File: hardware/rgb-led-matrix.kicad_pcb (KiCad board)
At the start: 2 copper layers, 75 x 55 mm, 153 parts, among them J1 AKL_5_2, P1 CONN_01X02, P2 CON-SENSOR, Q1 2N7002P, U1 XMC1XXX24, U2 DRILL, U3 DRILL, U4 DRILL, U5 DRILL

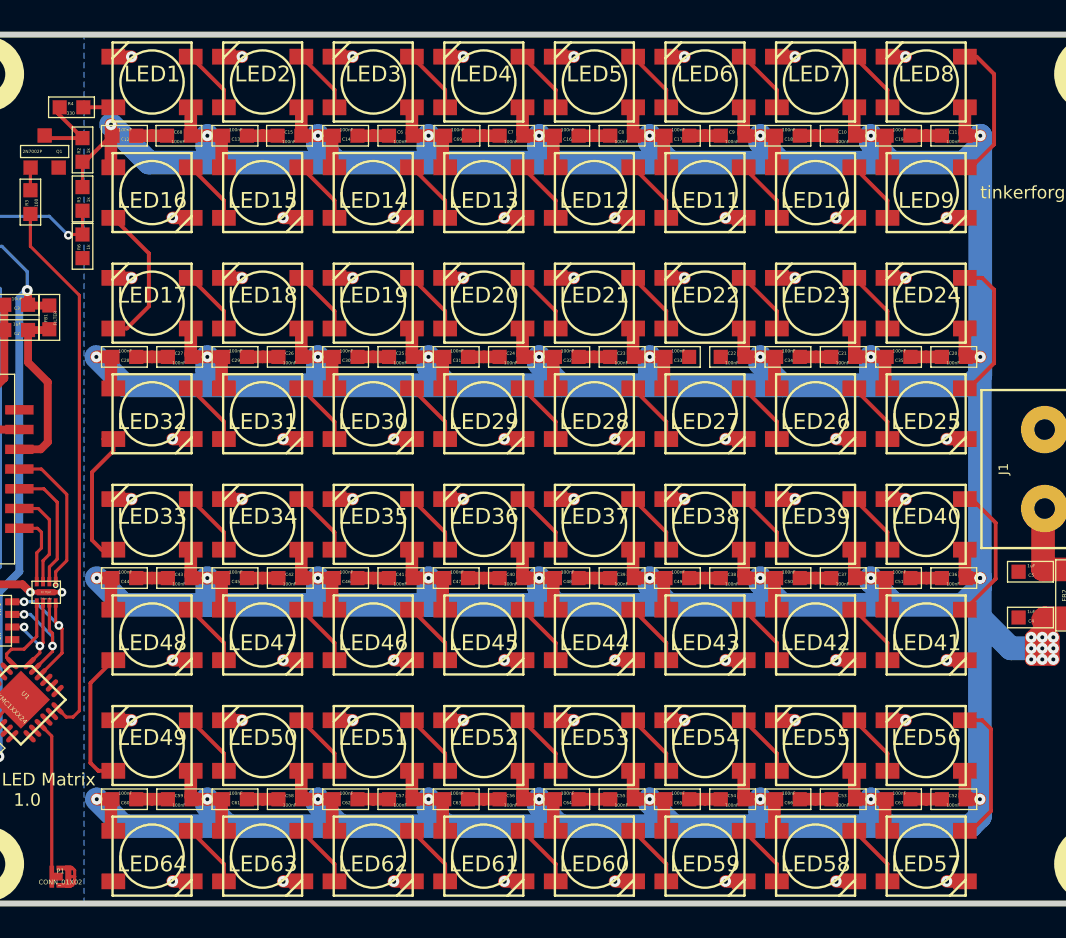
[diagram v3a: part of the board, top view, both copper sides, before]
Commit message: add vias for better cooling
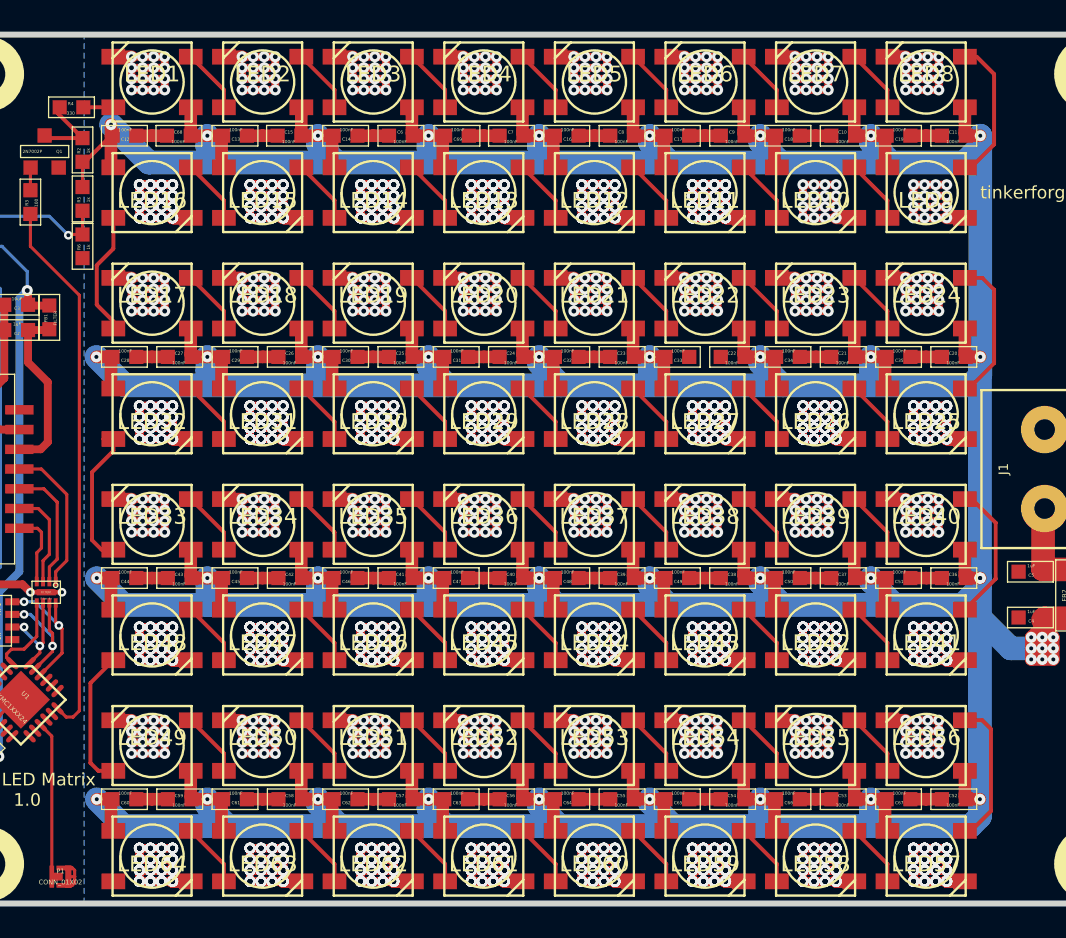
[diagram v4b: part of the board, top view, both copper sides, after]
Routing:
- net GND: track 160.4 -> 1880.9 mm, vias 71 -> 2471
- net Net-(LED16-Pad2): track 10.3 -> 8.82 mm

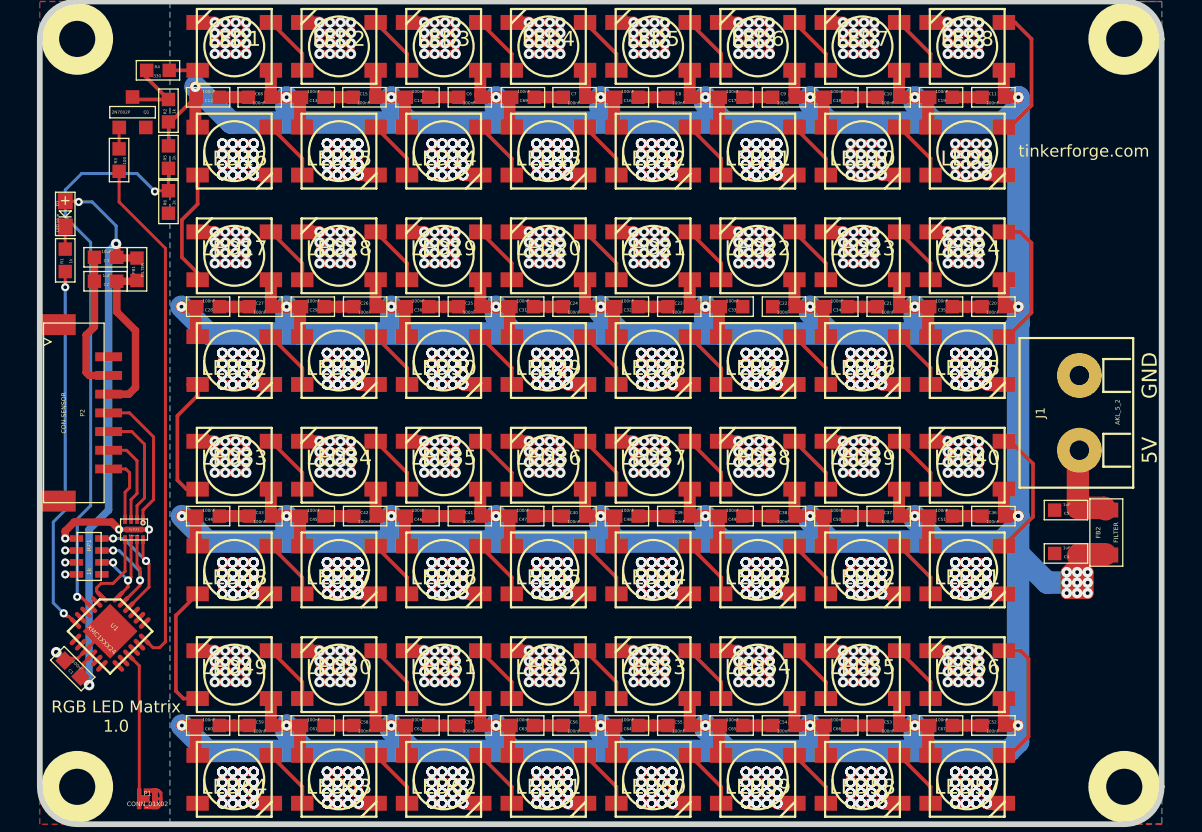
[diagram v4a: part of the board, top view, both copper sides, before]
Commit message: add fiducials and logos
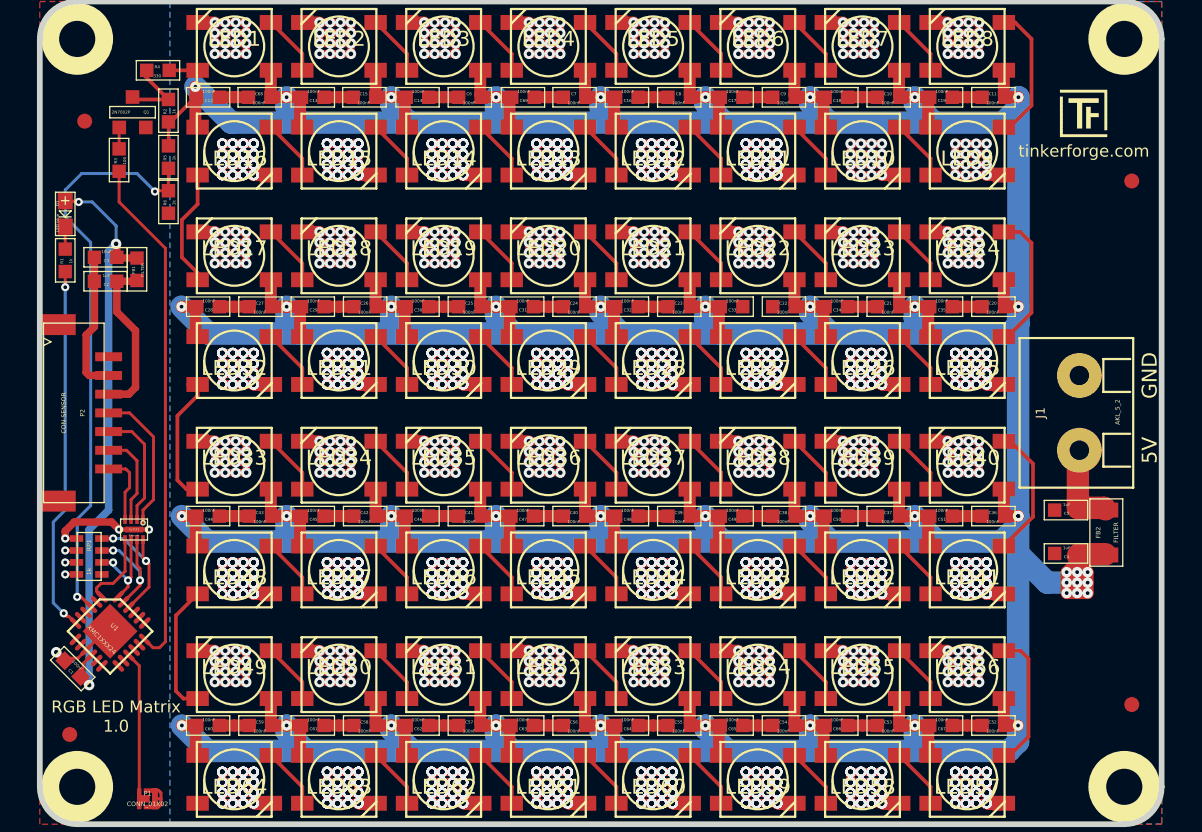
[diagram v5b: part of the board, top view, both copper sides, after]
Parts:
- added Fiducial_Mark: VAL**, kicad-libraries:Fiducial_Mark, F.Cu at (115.3, 62.3)
- added Fiducial_Mark: VAL**, kicad-libraries:Fiducial_Mark, F.Cu at (185.3, 66.3)
- added Fiducial_Mark: VAL**, kicad-libraries:Fiducial_Mark, F.Cu at (185.3, 101.3)
- added Fiducial_Mark: VAL**, kicad-libraries:Fiducial_Mark, F.Cu at (114.3, 103.3)
- added G***: Logo_31x31, kicad-libraries:Logo_31x31, F.Cu at (180.5, 60.2)
- added G***: LOGO, kicad-libraries:WEEE_7mm, B.Cu at (142.8, 81.8)
- added G***: LOGO, kicad-libraries:Logo_CoMCU, B.Cu at (149.8, 81.8)
- added VAL: CE_5mm, kicad-libraries:CE_5mm, B.Cu at (156.8, 81.8)

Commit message: remove old text
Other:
- board text added: "Copyright Tinkerforge GmbH 2017. This documentation describes Open Hardware and is licensed under the CERN OHL v. 1.1. You may redistribute and modify this documentation under the terms of the CERN OHL v.1.1. (http://ohwr.org/cernohl). This documentation is distributed WITHOUT ANY EXPRESS OR IMPLIED WARRANTY, INCLUDING OF MERCHANTABILITY, SATISFACTORY QUALITY AND FITNESS FOR A PARTICULAR PURPOSE.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"
- board text removed: "Copyright Tinkerforge GmbH 2015. This documentation describes Open Hardware and is licensed under the CERN OHL v. 1.1. You may redistribute and modify this documentation under the terms of the CERN OHL v.1.1. (http://ohwr.org/cernohl). This documentation is distributed WITHOUT ANY EXPRESS OR IMPLIED WARRANTY, INCLUDING OF MERCHANTABILITY, SATISFACTORY QUALITY AND FITNESS FOR A PARTICULAR PURPOSE.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"
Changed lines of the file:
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@@
   (page A4)
   (title_block
-    (title "RGB LED Bricklet")
-    (date "Mi 18 Nov 2015")
+    (title "RGB LED Matrix Bricklet")
+    (date 2017-02-08)
     (rev 1.0)
     (company "Tinkerforge GmbH")
     (comment 1 "Licensed under CERN OHL v.1.1")
-    (comment 2 "Copyright (©) 2015, B.Nordmeyer <bastian@tinkerforge.com>")
+    (comment 2 "Copyright (©) 2017, B.Nordmeyer <bastian@tinkerforge.com>")
   )
   (layers
@@
   (gr_arc (start 114.8 56.8) (end 112.3 56.8) (angle 90) (layer Edge.Cuts) (width 0.381))
   (gr_arc (start 114.8 106.8) (end 114.8 109.3) (angle 90) (layer Edge.Cuts) (width 0.381))
-  (gr_text "Copyright Tinkerforge GmbH 2015.\nThis documentation describes Open Hardware and is licensed under the\nCERN OHL v. 1.1.\nYou may redistribute and modify this documentation under the terms of the\nCERN OHL v.1.1. (http://ohwr.org/cernohl). This documentation is distributed\nWITHOUT ANY EXPRESS OR IMPLIED WARRANTY, INCLUDING OF\nMERCHANTABILITY, SATISFACTORY QUALITY AND FITNESS FOR A\nPARTICULAR PURPOSE. Please see the CERN OHL v.1.1 for applicable\nconditions" (at 258.8 156.55) (layer Cmts.User)
+  (gr_text "Copyright Tinkerforge GmbH 2017.\nThis documentation describes Open Hardware and is licensed under the\nCERN OHL v. 1.1.\nYou may redistribute and modify this documentation under the terms of the\nCERN OHL v.1.1. (http://ohwr.org/cernohl). This documentation is distributed\nWITHOUT ANY EXPRESS OR IMPLIED WARRANTY, INCLUDING OF\nMERCHANTABILITY, SATISFACTORY QUALITY AND FITNESS FOR A\nPARTICULAR PURPOSE. Please see the CERN OHL v.1.1 for applicable\nconditions" (at 258.8 156.55) (layer Cmts.User)
     (effects (font (size 0.8001 0.8001) (thickness 0.200025) italic))
   )

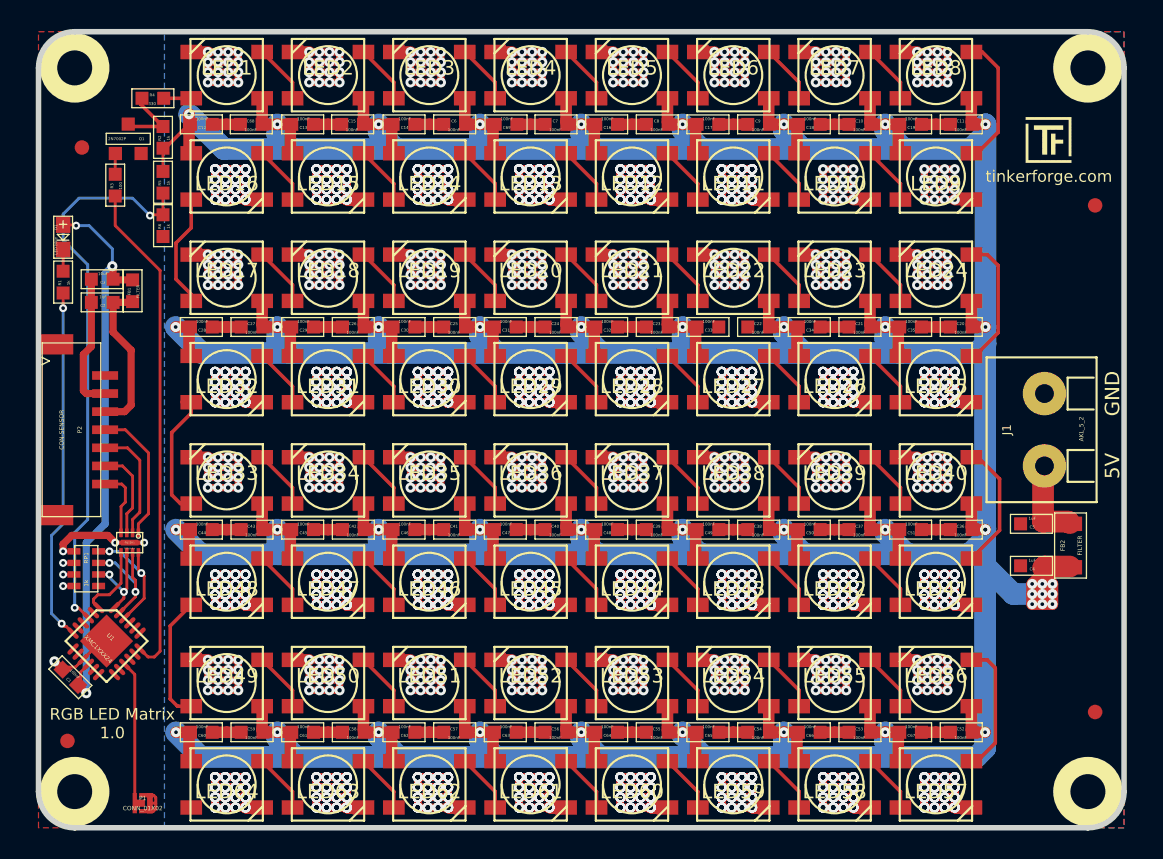
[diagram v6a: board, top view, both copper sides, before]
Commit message: fix spi filtering
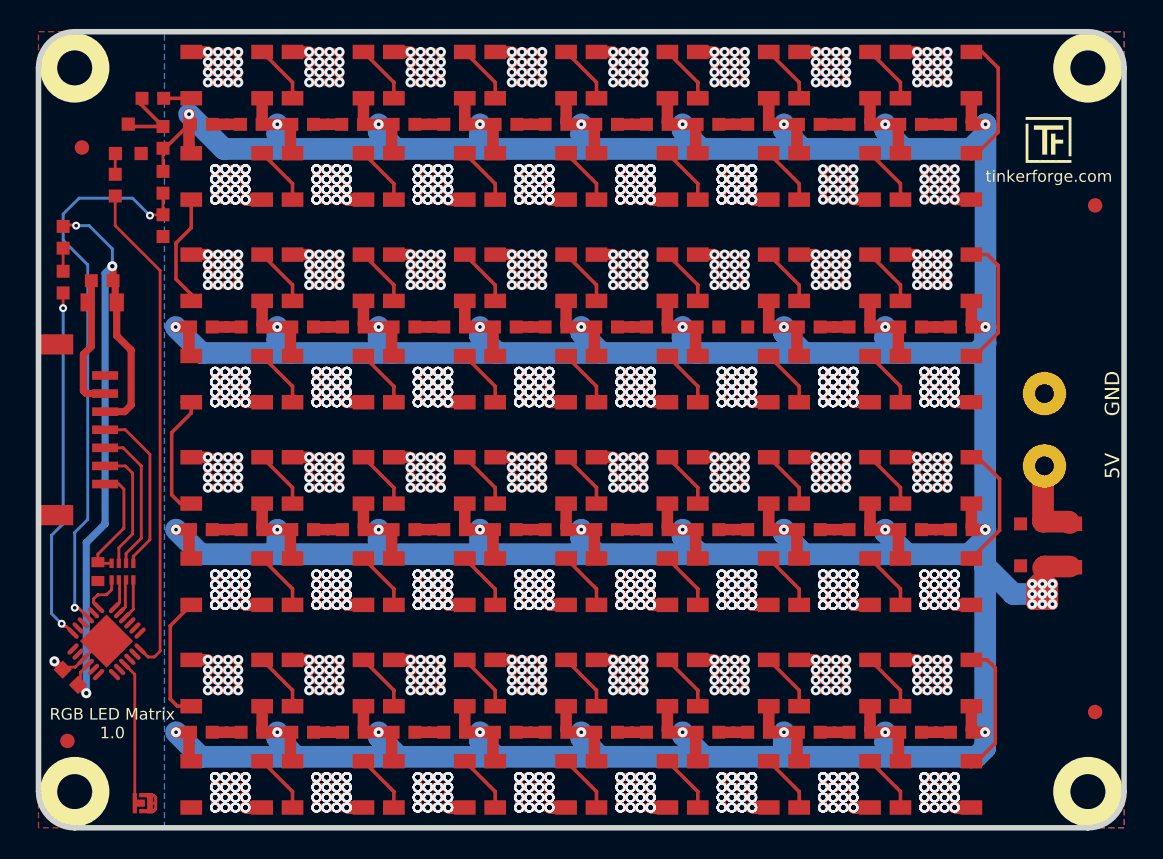
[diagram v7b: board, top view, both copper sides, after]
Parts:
- removed FB1: FILTER, kicad-libraries:0603F
- removed FILTER1: Filter-4x, kicad-libraries:DFN8-17x135
- added C70: TBD, kicad-libraries:C0402E, F.Cu at (116.4, 91.6)
- C1, C10, C11, C12, C13, C14, C15, C16, C17, C18, C19, C2, C20, C21, C22, C23, C24, C25, C26, C27, C28, C29, C30, C31, C32, C33, C34, C35, C36, C37, C38, C39, C4, C40, C41, C42, C43, C44, C45, C46, C47, C48, C49, C5, C50, C51, C52, C53, C54, C55, C56, C57, C58, C59, C6, C60, C61, C62, C63, C64, C65, C66, C67, C68, C69, C7, C8, C9: footprint kicad-libraries:0603F -> kicad-libraries:C0603F
- C3: footprint kicad-libraries:0603F -> kicad-libraries:C0805
- D1: footprint kicad-libraries:D0603E -> kicad-libraries:D0603F
- FB2: footprint kicad-libraries:1206 -> kicad-libraries:R1206
- R1, R2, R3, R4, R5, R6: footprint kicad-libraries:0603F -> kicad-libraries:R0603F
- RP1: value 1k -> TBD; footprint 0603X4 -> 4X0402
- moved RP1 2.51 mm to (118.1, 91.6), turned to 180 degrees
- moved C3 1.60 mm to (116.7, 73.0)
- moved C2 1.50 mm to (116.7, 71.5)
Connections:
- C2 pad 2: Net-(C2-Pad2) -> 3V3
- P2 pad 3: Net-(C2-Pad2) -> 3V3
- P2 pad 4: Net-(FILTER1-Pad1) -> Net-(P2-Pad4)
- P2 pad 5: Net-(FILTER1-Pad2) -> Net-(P2-Pad5)
- P2 pad 6: Net-(FILTER1-Pad3) -> Net-(P2-Pad6)
- P2 pad 7: Net-(FILTER1-Pad4) -> Net-(C70-Pad2)
- RP1 pad 1: (no net) -> Net-(P2-Pad4)
- RP1 pad 2: S-MOSI -> Net-(P2-Pad5)
- RP1 pad 3: S-CLK -> Net-(P2-Pad6)
- RP1 pad 4: S-CS -> Net-(C70-Pad2)
- RP1 pad 5: GND -> S-MISO
- RP1 pad 6: GND -> S-MOSI
- RP1 pad 7: GND -> S-CLK
- RP1 pad 8: GND -> S-CS
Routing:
- net Net-(P2-Pad4): track 0.00 -> 11.8 mm
- net Net-(C2-Pad2): track 11.0 -> 0.00 mm
- net Net-(P2-Pad5): track 0.00 -> 10.2 mm
- net 3V3: track 40.3 -> 50.1 mm
- net GND: track 1880.9 -> 1871.3 mm, vias 2471 -> 2465
- net Net-(FILTER1-Pad1): track 9.48 -> 0.00 mm
- net Net-(P2-Pad6): track 0.00 -> 8.73 mm
- net Net-(C70-Pad2): track 0.00 -> 8.22 mm
- net Net-(FILTER1-Pad2): track 7.98 -> 0.00 mm
- net Net-(FILTER1-Pad3): track 6.28 -> 0.00 mm
- net S-CLK: track 8.43 -> 2.45 mm, vias 2 -> 0
- net S-CS: track 8.81 -> 2.86 mm, vias 2 -> 0
- net Net-(FILTER1-Pad4): track 4.75 -> 0.00 mm
- net S-MOSI: track 6.53 -> 2.08 mm, vias 2 -> 0
- net S-MISO: track 5.21 -> 2.92 mm

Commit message: Fix CE logo
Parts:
- turned VAL to 0 degrees
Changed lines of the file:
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@@
-(kicad_pcb (version 4) (host pcbnew 4.0.2+e4-6225~38~ubuntu15.10.1-stable)
+(kicad_pcb (version 4) (host pcbnew 4.0.2+dfsg1-stable)
   (general
     (links 368)
     (no_connects 0)
-    (area 112.109499 54.109499 187.490501 109.490501)
+    (area 111.444999 53.444999 282.895869 162.490743)
     (thickness 1.6002)
     (drawings 15)
@@
     (aux_axis_origin 112.3 54.3)
     (grid_origin 112.3 54.3)
-    (visible_elements FFFF3FBF)
+    (visible_elements FFFFBFFF)
     (pcbplotparams
       (layerselection 0x00030_80000001)
@@
   )
   (module kicad-libraries:CE_5mm (layer Rückseite)
-    (at 156.8 81.8 180)
-    (fp_text reference VAL (at 0 0 180) (layer B.SilkS) hide
+    (at 156.8 81.8)
+    (fp_text reference VAL (at 0 0) (layer B.SilkS) hide
       (effects (font (size 1.143 1.143) (thickness 0.1778)) (justify mirror))
     )
-    (fp_text value CE_5mm (at 0 0 180) (layer B.SilkS) hide
+    (fp_text value CE_5mm (at 0 0) (layer B.SilkS) hide
       (effects (font (size 1.143 1.143) (thickness 0.1778)) (justify mirror))
     )
